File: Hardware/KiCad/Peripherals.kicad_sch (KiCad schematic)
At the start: 74 parts, among them Q1 PMBT3904, U1 MPU-6000, U2 HMC5883L, U3 FM24C64B, U4 BMP388

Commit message: Made a general PCB layout
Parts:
- U4: footprint PQFN50P200X200X80-10N -> flightController:PQFN50P200X200X80-10N
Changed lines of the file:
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@@
   (junction (at 267.97 29.845) (diameter 0) (color 0 0 0 0)
+  )
+  (junction (at 27.94 60.96) (diameter 0) (color 0 0 0 0)
   )
   (junction (at 201.93 128.905) (diameter 0) (color 0 0 0 0)
@@
     (stroke (width 0) (type default) (color 0 0 0 0))
   )
+  (wire (pts (xy 27.94 60.96) (xy 27.94 55.88))
+    (stroke (width 0) (type default) (color 0 0 0 0))
+  )
   (polyline (pts (xy 17.145 143.51) (xy 17.145 95.25))
     (stroke (width 0) (type default) (color 0 0 0 0))
@@
   )
   (wire (pts (xy 57.785 121.285) (xy 57.785 123.19))
+    (stroke (width 0) (type default) (color 0 0 0 0))
+  )
+  (wire (pts (xy 27.94 55.88) (xy 30.48 55.88))
     (stroke (width 0) (type default) (color 0 0 0 0))
   )
@@
     )
   )
-  (global_label "IMU_CS" (shape input) (at 76.835 34.925 90) (fields_autoplaced)
-    (effects (font (size 1.27 1.27)) (justify left))
-    (property "Intersheet References" "${INTERSHEET_REFS}" (id 0) (at 76.9144 25.6781 90)
-      (effects (font (size 1.27 1.27)) (justify left) hide)
-    )
-  )
   (global_label "IMU_MOSI" (shape input) (at 30.48 48.26 180) (fields_autoplaced)
     (effects (font (size 1.27 1.27)) (justify right))
@@
     (effects (font (size 1.27 1.27)) (justify right))
     (property "Intersheet References" "${INTERSHEET_REFS}" (id 0) (at 219.2321 46.2756 0)
-      (effects (font (size 1.27 1.27)) (justify right) hide)
-    )
-  )
-  (global_label "IMU_CS" (shape input) (at 30.48 55.88 180) (fields_autoplaced)
-    (effects (font (size 1.27 1.27)) (justify right))
-    (property "Intersheet References" "${INTERSHEET_REFS}" (id 0) (at 21.2331 55.8006 0)
       (effects (font (size 1.27 1.27)) (justify right) hide)
     )
@@
     (pin "8")
     (pin "9")
-  )
-  (symbol (lib_id "power:GND") (at 76.835 34.925 0) (unit 1)
-    (in_bom yes) (on_board yes) (fields_autoplaced)
-    (property "Reference" "#PWR0169" (id 0) (at 76.835 41.275 0)
-      (effects (font (size 1.27 1.27)) hide)
-    )
-    (property "Value" "GND" (id 1) (at 76.835 39.4875 0))
-    (property "Footprint" "" (id 2) (at 76.835 34.925 0)
-      (effects (font (size 1.27 1.27)) hide)
-    )
-    (property "Datasheet" "" (id 3) (at 76.835 34.925 0)
-      (effects (font (size 1.27 1.27)) hide)
-    )
-    (pin "1")
   )
   (symbol (lib_id "Device:FerriteBead_Small") (at 53.975 27.94 270) (unit 1)
@@
     (property "Reference" "U4" (id 0) (at 241.3 29.6885 0))
     (property "Value" "BMP388" (id 1) (at 241.3 32.4636 0))
-    (property "Footprint" "PQFN50P200X200X80-10N" (id 2) (at 241.3 48.895 0)
+    (property "Footprint" "flightController:PQFN50P200X200X80-10N" (id 2) (at 241.3 48.895 0)
       (effects (font (size 1.27 1.27)) (justify left bottom) hide)
     )

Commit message: Almost finished all routing
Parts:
- R1, R3, R4, R5, R7, R8: footprint Resistor_SMD:R_0603_1608Metric -> Resistor_SMD:R_0402_1005Metric
- TP1, TP10, TP11, TP12, TP13, TP14, TP15, TP16, TP17, TP18, TP19, TP2, TP20, TP21, TP22, TP23, TP24, TP25, TP26, TP27, TP28, TP29, TP3, TP30, TP31, TP4, TP5, TP6, TP7, TP8, TP9: footprint TestPoint:TestPoint_Pad_D1.5mm -> TestPoint:TestPoint_Pad_D1.0mm

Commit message: Routing finished
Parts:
- removed TP1, TP10, TP11, TP12, TP2, TP27, TP7, TP8, TP9: TestPoint, TestPoint:TestPoint_Pad_D1.0mm, symbol Connector:TestPoint

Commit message: Added labels
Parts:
- U2: footprint Package_LGA:LGA-16_3x3mm_P0.5mm -> flightController:LGA-16_3x3mm_P0.5mm_Large_Pads
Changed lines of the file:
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@@
       (effects (font (size 1.27 1.27)) (justify left))
     )
-    (property "Footprint" "Package_LGA:LGA-16_3x3mm_P0.5mm" (id 2) (at 122.555 69.85 0)
+    (property "Footprint" "flightController:LGA-16_3x3mm_P0.5mm_Large_Pads" (id 2) (at 122.555 69.85 0)
       (effects (font (size 1.27 1.27)) hide)
     )

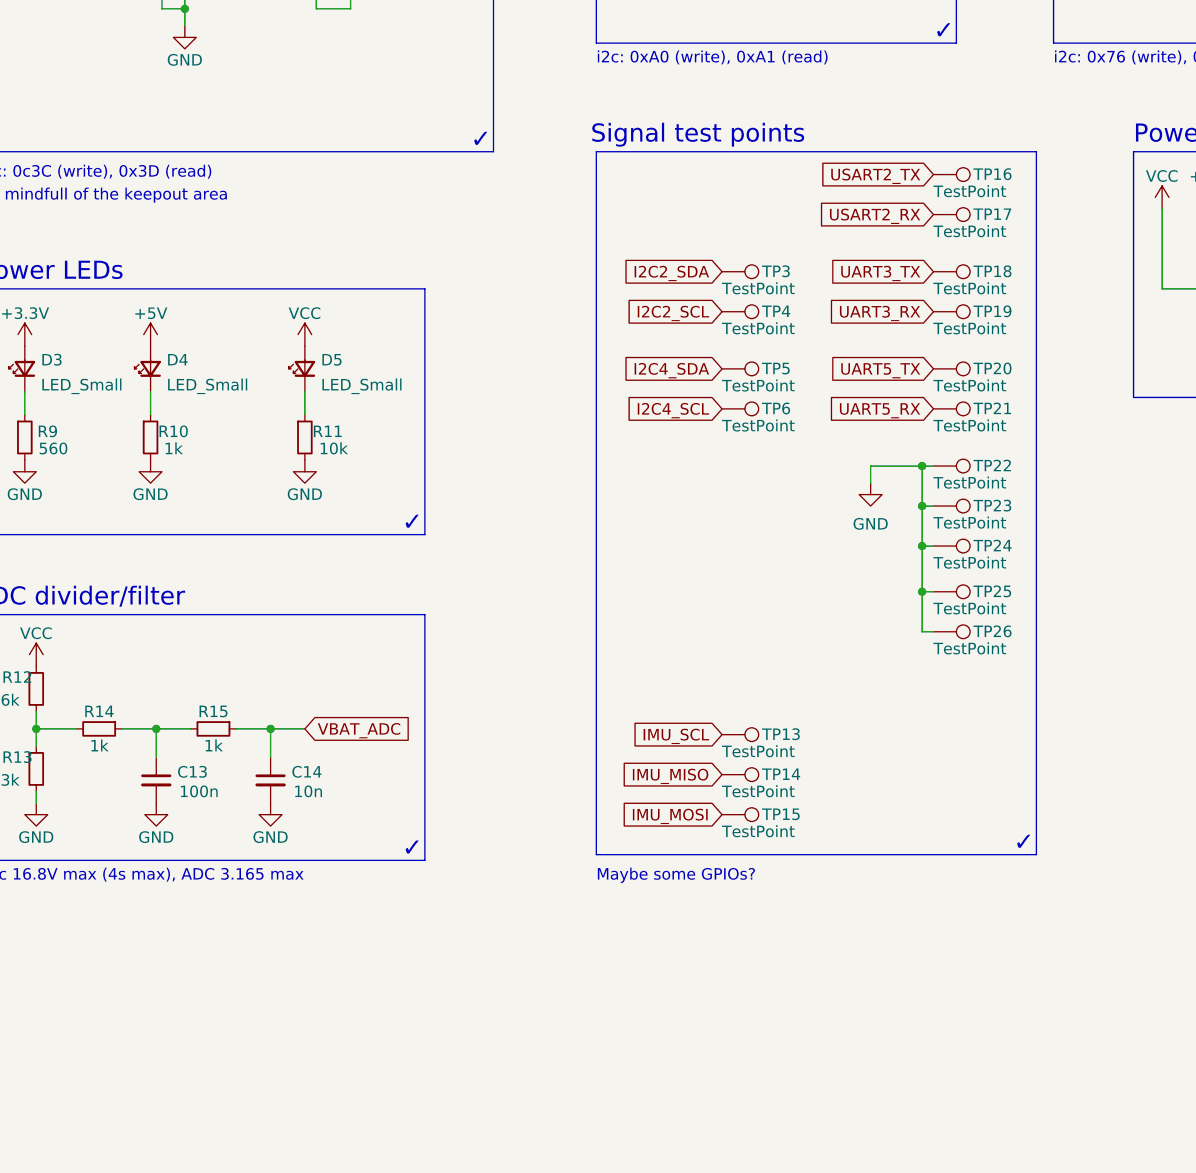
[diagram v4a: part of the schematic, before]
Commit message: Some small trace and layout optimisation
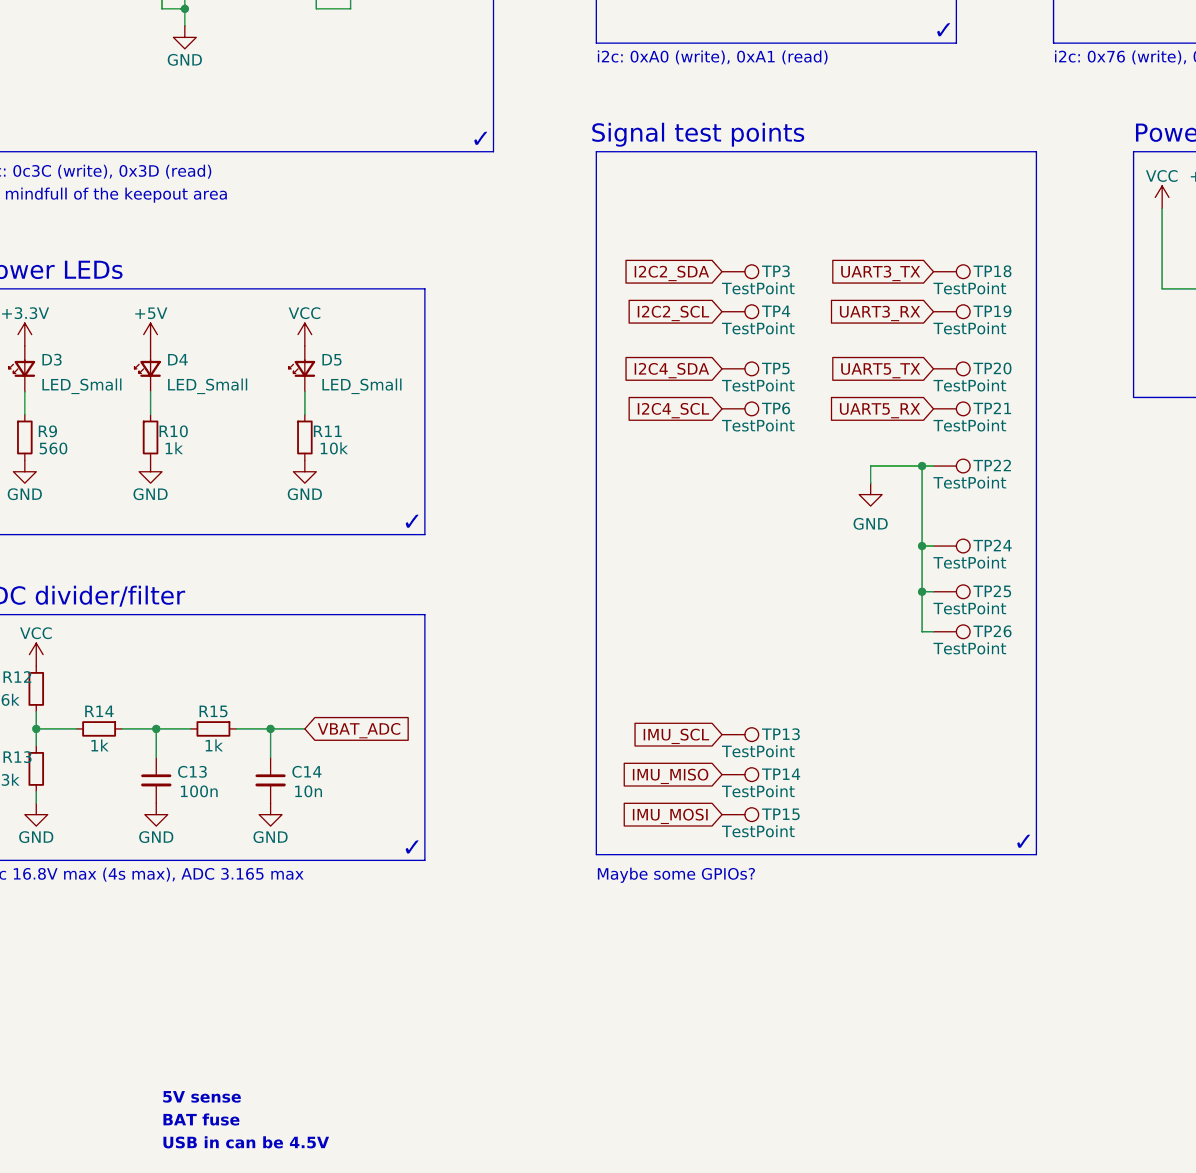
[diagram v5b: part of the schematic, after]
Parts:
- removed TP16, TP17, TP23: TestPoint, TestPoint:TestPoint_Pad_D1.0mm, symbol Connector:TestPoint
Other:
- note added: "5V sense"
- note added: "BAT fuse"
- note added: "USB in can be 4.5V"
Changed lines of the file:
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@@
   (junction (at 255.905 56.515) (diameter 0) (color 0 0 0 0)
-  )
-  (junction (at 201.93 119.38) (diameter 0) (color 0 0 0 0)
   )
   (junction (at 259.715 29.845) (diameter 0) (color 0 0 0 0)
@@
     (stroke (width 0) (type default) (color 0 0 0 0))
   )
-  (wire (pts (xy 203.2 119.38) (xy 201.93 119.38))
-    (stroke (width 0) (type default) (color 0 0 0 0))
-  )
   (wire (pts (xy 78.105 60.96) (xy 78.105 65.405))
     (stroke (width 0) (type default) (color 0 0 0 0))
@@
     (stroke (width 0) (type default) (color 0 0 0 0))
   )
-  (wire (pts (xy 201.93 119.38) (xy 201.93 114.935))
+  (wire (pts (xy 201.93 114.935) (xy 201.93 123.825))
     (stroke (width 0) (type default) (color 0 0 0 0))
   )
@@
   )
   (polyline (pts (xy 214.63 80.01) (xy 165.735 80.01))
-    (stroke (width 0) (type default) (color 0 0 0 0))
-  )
-  (wire (pts (xy 201.93 119.38) (xy 201.93 123.825))
     (stroke (width 0) (type default) (color 0 0 0 0))
   )
@@
   (text "✓" (at 151.765 80.01 0)
     (effects (font (size 2 2)) (justify left bottom))
+  )
+  (text "5V sense" (at 117.475 186.055 0)
+    (effects (font (size 1.27 1.27) (thickness 0.254) bold) (justify left bottom))
   )
   (text "ADC divider/filter" (at 96.52 130.81 0)
@@
     (effects (font (size 1.27 1.27)) (justify left bottom))
   )
+  (text "USB in can be 4.5V" (at 117.475 191.135 0)
+    (effects (font (size 1.27 1.27) (thickness 0.254) bold) (justify left bottom))
+  )
   (text "CPOUT = 2.2nF 50V" (at 17.145 82.55 0)
     (effects (font (size 1.27 1.27)) (justify left bottom))
+  )
+  (text "BAT fuse" (at 117.475 188.595 0)
+    (effects (font (size 1.27 1.27) (thickness 0.254) bold) (justify left bottom))
   )
   (text "✓" (at 203.2 67.945 0)
@@
     )
   )
-  (global_label "USART2_TX" (shape input) (at 203.2 82.55 180) (fields_autoplaced)
-    (effects (font (size 1.27 1.27)) (justify right))
-    (property "Intersheet References" "${INTERSHEET_REFS}" (id 0) (at 189.8407 82.4706 0)
-      (effects (font (size 1.27 1.27)) (justify right) hide)
-    )
-  )
   (global_label "BUZZ_ON" (shape input) (at 31.75 170.815 180) (fields_autoplaced)
     (effects (font (size 1.27 1.27)) (justify right))
@@
     (effects (font (size 1.27 1.27)) (justify right))
     (property "Intersheet References" "${INTERSHEET_REFS}" (id 0) (at 190.2036 102.1556 0)
-      (effects (font (size 1.27 1.27)) (justify right) hide)
-    )
-  )
-  (global_label "USART2_RX" (shape input) (at 203.2 86.995 180) (fields_autoplaced)
-    (effects (font (size 1.27 1.27)) (justify right))
-    (property "Intersheet References" "${INTERSHEET_REFS}" (id 0) (at 189.5383 86.9156 0)
       (effects (font (size 1.27 1.27)) (justify right) hide)
     )
@@
     )
     (property "Datasheet" "~" (id 3) (at 179.705 102.87 0)
-      (effects (font (size 1.27 1.27)) hide)
-    )
-    (pin "1")
-  )
-  (symbol (lib_id "Connector:TestPoint") (at 203.2 119.38 270) (unit 1)
-    (in_bom yes) (on_board yes)
-    (property "Reference" "TP23" (id 0) (at 207.645 119.38 90)
-      (effects (font (size 1.27 1.27)) (justify left))
-    )
-    (property "Value" "TestPoint" (id 1) (at 203.2 121.285 90)
-      (effects (font (size 1.27 1.27)) (justify left))
-    )
-    (property "Footprint" "TestPoint:TestPoint_Pad_D1.0mm" (id 2) (at 203.2 124.46 0)
-      (effects (font (size 1.27 1.27)) hide)
-    )
-    (property "Datasheet" "~" (id 3) (at 203.2 124.46 0)
       (effects (font (size 1.27 1.27)) hide)
     )
@@
     (pin "1")
   )
-  (symbol (lib_id "Connector:TestPoint") (at 203.2 86.995 270) (unit 1)
-    (in_bom yes) (on_board yes)
-    (property "Reference" "TP17" (id 0) (at 207.645 86.995 90)
-      (effects (font (size 1.27 1.27)) (justify left))
-    )
-    (property "Value" "TestPoint" (id 1) (at 203.2 88.9 90)
-      (effects (font (size 1.27 1.27)) (justify left))
-    )
-    (property "Footprint" "TestPoint:TestPoint_Pad_D1.0mm" (id 2) (at 203.2 92.075 0)
-      (effects (font (size 1.27 1.27)) hide)
-    )
-    (property "Datasheet" "~" (id 3) (at 203.2 92.075 0)
-      (effects (font (size 1.27 1.27)) hide)
-    )
-    (pin "1")
-  )
   (symbol (lib_id "power:GND") (at 267.97 36.83 0) (unit 1)
     (in_bom yes) (on_board yes)
@@
       (effects (font (size 1.27 1.27)) hide)
     )
-    (pin "1")
-  )
-  (symbol (lib_id "Connector:TestPoint") (at 203.2 82.55 270) (unit 1)
-    (in_bom yes) (on_board yes)
-    (property "Reference" "TP16" (id 0) (at 207.645 82.55 90)
-      (effects (font (size 1.27 1.27)) (justify left))
-    )
-    (property "Value" "TestPoint" (id 1) (at 203.2 84.455 90)
-      (effects (font (size 1.27 1.27)) (justify left))
-    )
-    (property "Footprint" "TestPoint:TestPoint_Pad_D1.0mm" (id 2) (at 203.2 87.63 0)
-      (effects (font (size 1.27 1.27)) hide)
-    )
-    (property "Datasheet" "~" (id 3) (at 203.2 87.63 0)
-      (effects (font (size 1.27 1.27)) hide)
-    )

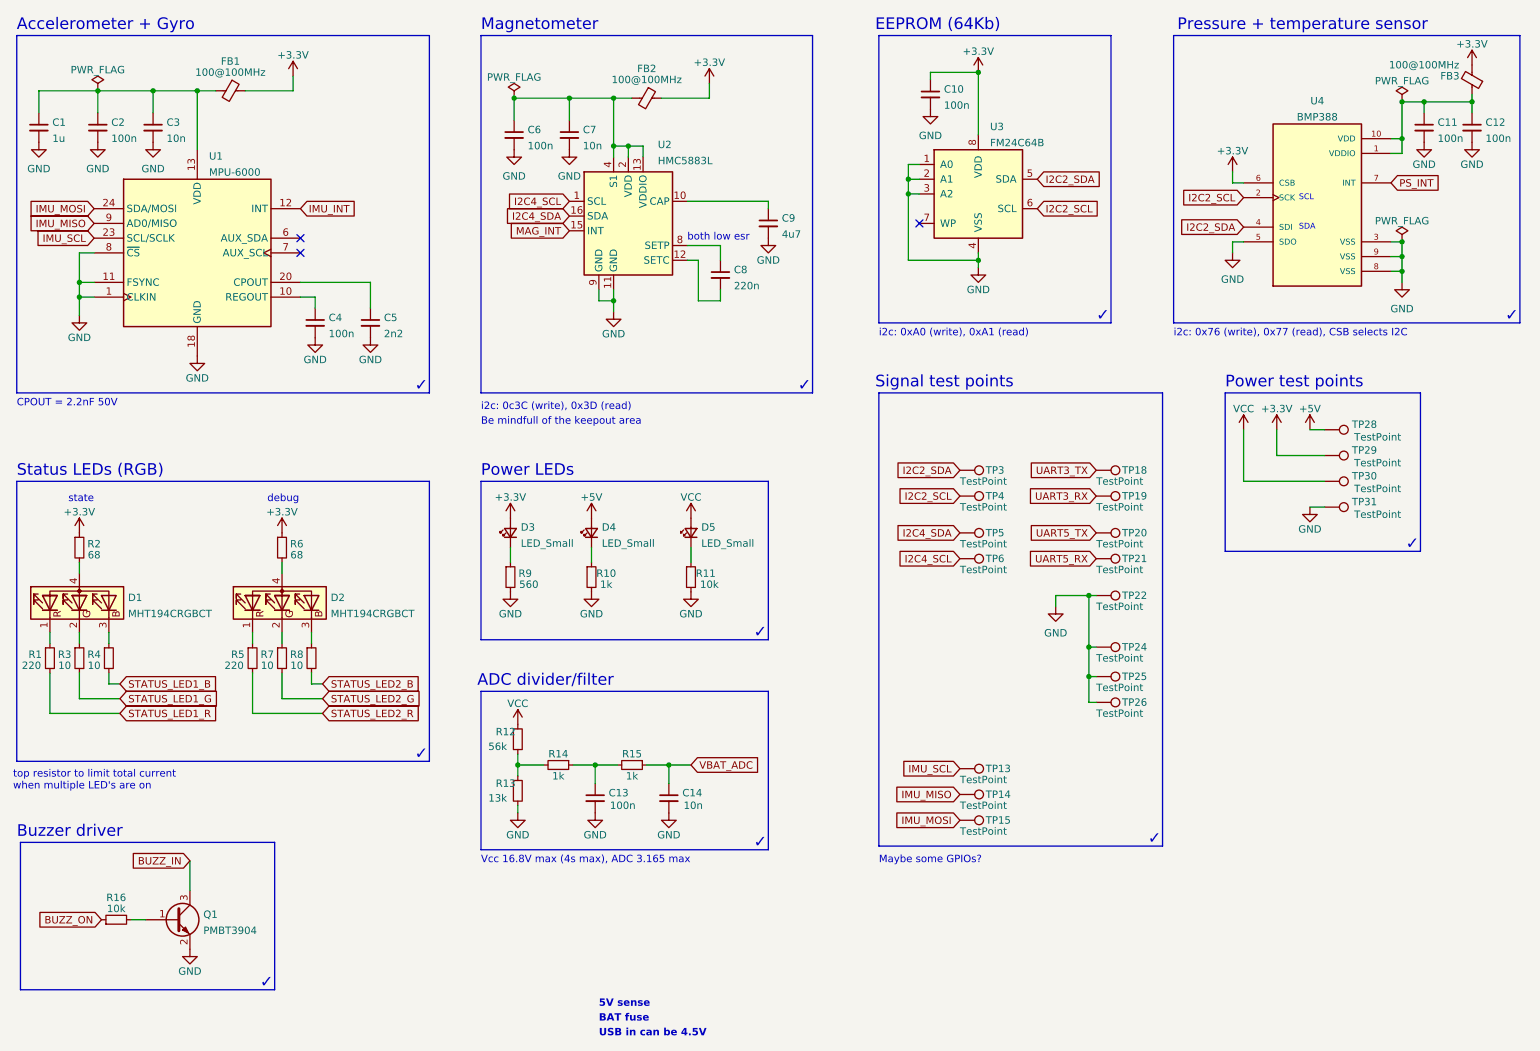
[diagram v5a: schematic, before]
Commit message: Added a 5V sense line
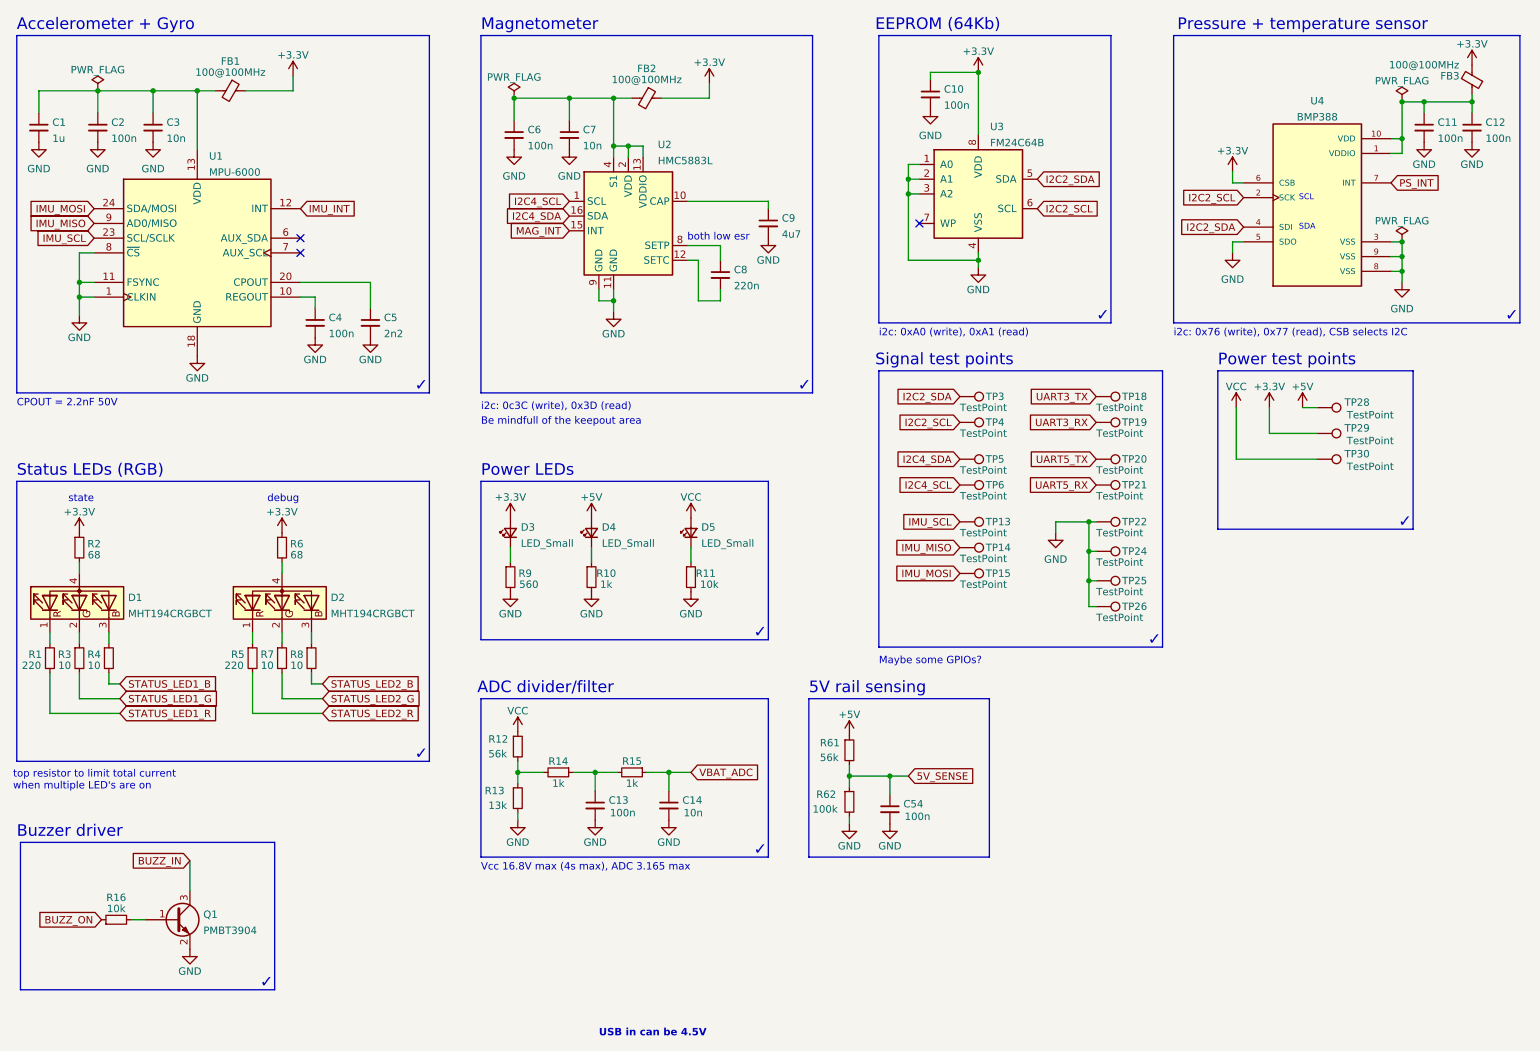
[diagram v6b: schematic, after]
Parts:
- removed TP31: TestPoint, TestPoint:TestPoint_Pad_D1.0mm, symbol Connector:TestPoint
- added C54: 100n, Capacitor_SMD:C_0402_1005Metric, symbol Device:C_Small
- added R61: 56k, Resistor_SMD:R_0402_1005Metric, symbol Device:R_Small
- added R62: 100k, Resistor_SMD:R_0402_1005Metric, symbol Device:R_Small
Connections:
- net +5V: now also R61.1
- net GND: now also C54.2, R62.2
- new net 5V_SENSE: C54.1, R61.2, R62.1
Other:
- note added: "5V rail sensing"
- note removed: "5V sense"
- note removed: "BAT fuse"
- moved on the sheet: C13, C14, R12, R13, R14, R15, TP13, TP14, TP15, TP18, TP19, TP20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
